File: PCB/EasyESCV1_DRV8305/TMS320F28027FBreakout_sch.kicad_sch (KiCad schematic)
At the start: 1 part, among them U2 TMS320F28027FPTT

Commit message: Finished REV1 Schematic Awaiting Review
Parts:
- added C18: 0.1U, symbol Device:C
- added C19, C20, C21: 2.2n, symbol Device:C
- added C26, C27, C29, C30: 2.2u, symbol Device:C
- added COM: TestPoint, symbol Connector:TestPoint
- added D2: GREEN, symbol Device:LED
- added FB1, FB2: 600, symbol Device:FerriteBead
- added J2: TC2050-IDC, Connector:Tag-Connect_TC2050-IDC-NL_2x05_P1.27mm_Vertical, symbol Connectors:TC2050-IDC
- added R12, R13, R14, R20: 47K, symbol Device:R_US
- added R21: 2.2K, symbol Device:R_US
- added R22: 10K, symbol Device:R_US
- added R23: 330, symbol Device:R_US
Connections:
- net VSEN_PVDD: now reaches U2.10 (ADCINA0_VREFHI)
- net VDDA: now reaches U2.11 (VDDA)
- net VDDA: now also C27.1, FB2.2
- net GND: now reaches U2.12 (VSSA_VREFLO)
- net GND: now also U2.33 (VSS), U2.34 (VREGENZ_N), U2.44 (VSS), U2.45 (X1), C18.2, C19.2, C20.2, C21.2, C26.2, C27.2, C29.2, C30.2, J2.3 (Pin_3), J2.5 (Pin_5), R21.2, R23.2
- net MCU_ISEN_A: now reaches U2.13 (ADCINB1)
- net MCU_ISEN_A: now also C19.1, R12.2
- net MCU_ISEN_B: now reaches U2.15 (ADCINB3)
- net MCU_ISEN_B: now also C20.1, R13.2
- net MCU_ISEN_C: now reaches U2.18 (ADCINB7)
- net MCU_ISEN_C: now also C21.1, R14.2
- net LED: now reaches U2.19 (GPIO34_COMP2OUT)
- net LED: now also D2.2 (A)
- net nTRST: now reaches U2.2 (TRST_N)
- net nTRST: now also J2.9 (Pin_9), R21.1
- net TDI: now reaches U2.20 (GPIO35_TDI)
- net TDI: now also J2.8 (Pin_8)
- net TMS: now reaches U2.21 (GPIO36_TMS)
- net TMS: now also J2.2 (Pin_2)
- net TDO: now reaches U2.22 (GPIO37_TDO)
- net TDO: now also J2.6 (Pin_6)
- net TCK: now reaches U2.23 (GPIO38_XCLKIN_TCK)
- net TCK: now also J2.4 (Pin_4)
- net SCLK: now reaches U2.24 (GPIO18_SPICLKA_SCITXDA_XCLKOUT)
- net COM: now reaches U2.25 (GPIO19_XCLKIN_SPISTEA_SCIRXDA_ECAP1_N)
- net COM: now also COM.1
- net SDO: now reaches U2.26 (GPIO17_SPISOMIA_TZ3_N)
- net SDI: now reaches U2.27 (GPIO16_SPISIMOA_TZ2_N)
- net INL_A: now reaches U2.28 (GPIO1_EPWM1B_COMP1OUT)
- net INH_A: now reaches U2.29 (GPIO0_EPWM1A)
- net nXRS: now reaches U2.3 (XRS_N)
- net nXRS: now also C18.1, R20.2
- net at U2.32 (VDD): now also C29.1
- net VDDIO: now reaches U2.35 (VDDIO)
- net VDDIO: now also C26.1, FB1.2
- net nSCS: now reaches U2.36 (GPIO33_SCLA_EPWMSYNCO_ADCSOCBO_N)
- net INH_B: now reaches U2.37 (GPIO2_EPWM2A)
- net INL_B: now reaches U2.38 (GPIO3_EPWM2B_COMP2OUT)
- net INH_C: now reaches U2.39 (GPIO4_EPWM3A)
- net INL_C: now reaches U2.40 (GPIO5_EPWM3B_ECAP1)
- net EN_GATE: now reaches U2.41 (GPIO6_EPWM4A_EPWMSYNCI_EPWMSYNCO)
- net WAKE: now reaches U2.42 (GPIO7_EPWM4B_SCIRXDA)
- net at U2.43 (VDD): now also C30.1
- net nFAULT: now reaches U2.48 (GPIO28_SCIRXDA_SDAA_TZ2_N)
- net nFAULT: now also R22.2
- net VSEN_A: now reaches U2.6 (ADCINA7)
- net VSEN_B: now reaches U2.7 (ADCINA3)
- net VSEN_C: now reaches U2.8 (ADCINA1)
- new net: D2.1 (K), R23.1
- new net 3.3V: FB1.1, FB2.1, J2.1 (Pin_1), R20.1, R22.1
- new net ISEN_A: R12.1
- new net ISEN_B: R13.1
- new net ISEN_C: R14.1
- no-connect marks 0 -> 13
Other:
- note added: "Current Sense"
- note added: "JTAG"
- note added: "MCU Power"
- note added: "Microcontroller"
- note added: "Reset"
- note added: "Status"
- company: (none) -> Buckley Boards 
- title: (none) -> Easy ESC
- moved on the sheet: U2

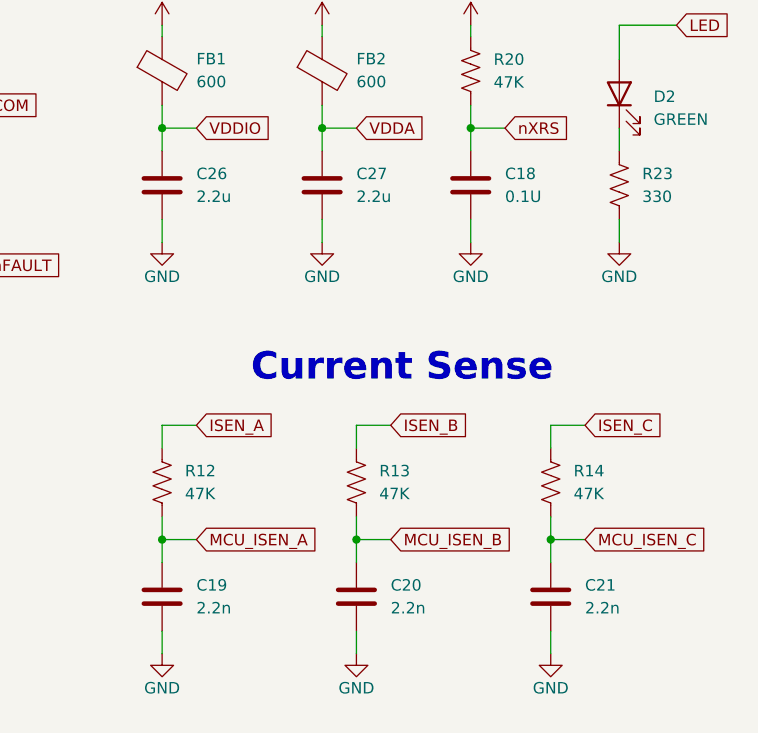
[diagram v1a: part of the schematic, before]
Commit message: Updated Some Errors in Schematic
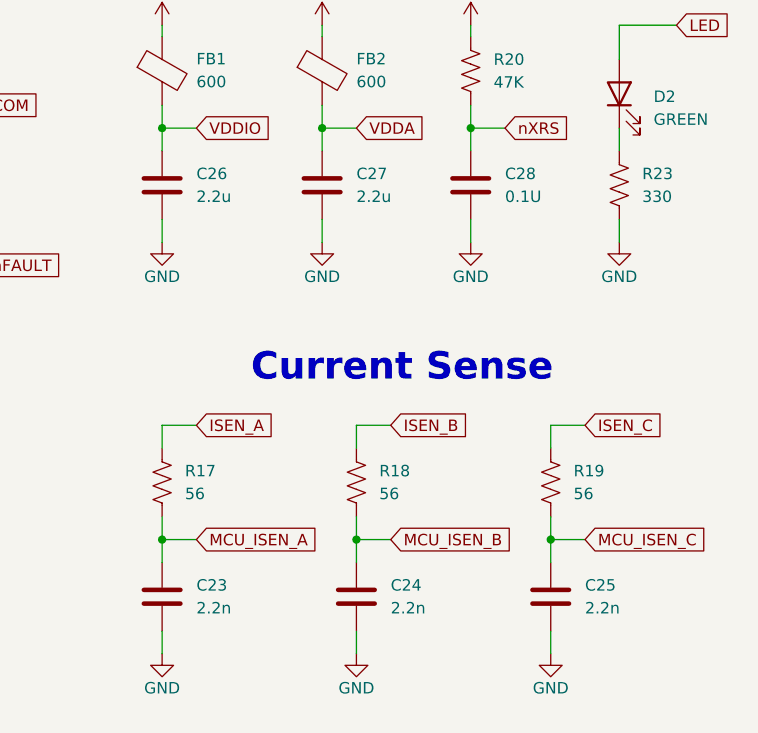
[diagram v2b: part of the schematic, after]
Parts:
- R17: renamed from R12; value 47K -> 56
- R18: renamed from R13; value 47K -> 56
- R19: renamed from R14; value 47K -> 56
- renumbered C19 to C23, C20 to C24, C21 to C25, C18 to C28
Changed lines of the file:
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@@
 		(dnp no)
 		(fields_autoplaced yes)
-		(property "Reference" "R14"
+		(property "Reference" "R19"
 			(at 256.54 128.2699 0)
 			(effects
@@
 			)
 		)
-		(property "Value" "47K"
+		(property "Value" "56"
 			(at 256.54 130.8099 0)
 			(effects
@@
 			(project "EasyESCV1_DRV8305"
 				(path "/6c304649-7c80-4a4c-b925-07b9210ad53d/8049925a-2faa-4187-b86e-b6208aed2e10"
-					(reference "R14")
+					(reference "R19")
 					(unit 1)
 				)
@@
 		(dnp no)
 		(fields_autoplaced yes)
-		(property "Reference" "C19"
+		(property "Reference" "C23"
 			(at 214.63 140.9699 0)
 			(effects
@@
 			(project "EasyESCV1_DRV8305"
 				(path "/6c304649-7c80-4a4c-b925-07b9210ad53d/8049925a-2faa-4187-b86e-b6208aed2e10"
-					(reference "C19")
+					(reference "C23")
 					(unit 1)
 				)
@@
 		(dnp no)
 		(fields_autoplaced yes)
-		(property "Reference" "R13"
+		(property "Reference" "R18"
 			(at 234.95 128.2699 0)
 			(effects
@@
 			)
 		)
-		(property "Value" "47K"
+		(property "Value" "56"
 			(at 234.95 130.8099 0)
 			(effects
@@
 			(project "EasyESCV1_DRV8305"
 				(path "/6c304649-7c80-4a4c-b925-07b9210ad53d/8049925a-2faa-4187-b86e-b6208aed2e10"
-					(reference "R13")
+					(reference "R18")
 					(unit 1)
 				)
@@
 		(dnp no)
 		(fields_autoplaced yes)
-		(property "Reference" "C20"
+		(property "Reference" "C24"
 			(at 236.22 140.9699 0)
 			(effects
@@
 			(project "EasyESCV1_DRV8305"
 				(path "/6c304649-7c80-4a4c-b925-07b9210ad53d/8049925a-2faa-4187-b86e-b6208aed2e10"
-					(reference "C20")
+					(reference "C24")
 					(unit 1)
 				)
@@
 		(dnp no)
 		(fields_autoplaced yes)
-		(property "Reference" "C18"
+		(property "Reference" "C28"
 			(at 248.92 95.2499 0)
 			(effects
@@
 			(project "EasyESCV1_DRV8305"
 				(path "/6c304649-7c80-4a4c-b925-07b9210ad53d/8049925a-2faa-4187-b86e-b6208aed2e10"
-					(reference "C18")
+					(reference "C28")
 					(unit 1)
 				)
@@
 		(dnp no)
 		(fields_autoplaced yes)
-		(property "Reference" "R12"
+		(property "Reference" "R17"
 			(at 213.36 128.2699 0)
 			(effects
@@
 			)
 		)
-		(property "Value" "47K"
+		(property "Value" "56"
 			(at 213.36 130.8099 0)
 			(effects
@@
 			(project "EasyESCV1_DRV8305"
 				(path "/6c304649-7c80-4a4c-b925-07b9210ad53d/8049925a-2faa-4187-b86e-b6208aed2e10"
-					(reference "R12")
+					(reference "R17")
 					(unit 1)
 				)
@@
 		(dnp no)
 		(fields_autoplaced yes)
-		(property "Reference" "C21"
+		(property "Reference" "C25"
 			(at 257.81 140.9699 0)
 			(effects
@@
 			(project "EasyESCV1_DRV8305"
 				(path "/6c304649-7c80-4a4c-b925-07b9210ad53d/8049925a-2faa-4187-b86e-b6208aed2e10"
-					(reference "C21")
-					(unit 1)
-				)
+					(reference "C25")
+					(unit 1)
+				)

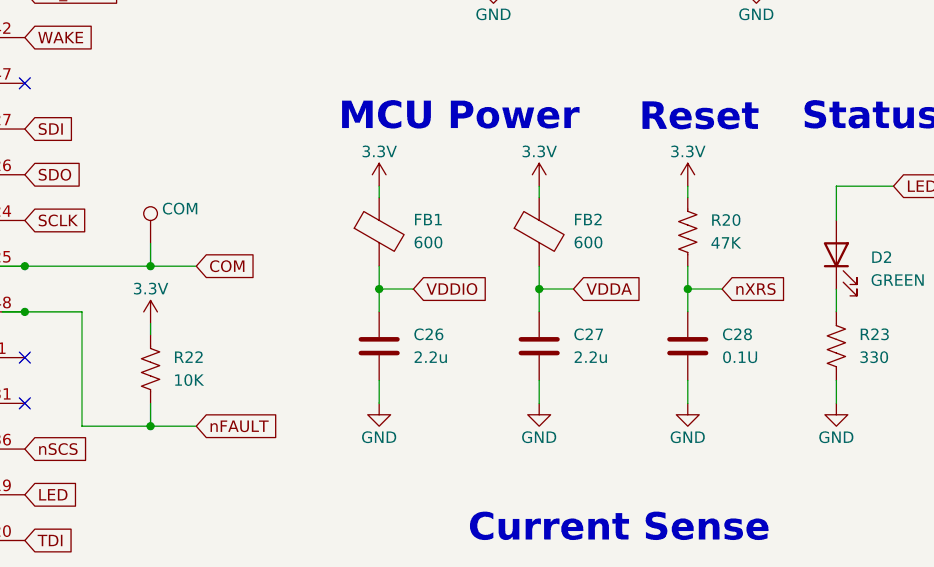
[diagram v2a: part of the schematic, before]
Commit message: Fixed issue with fet symbol and started layout
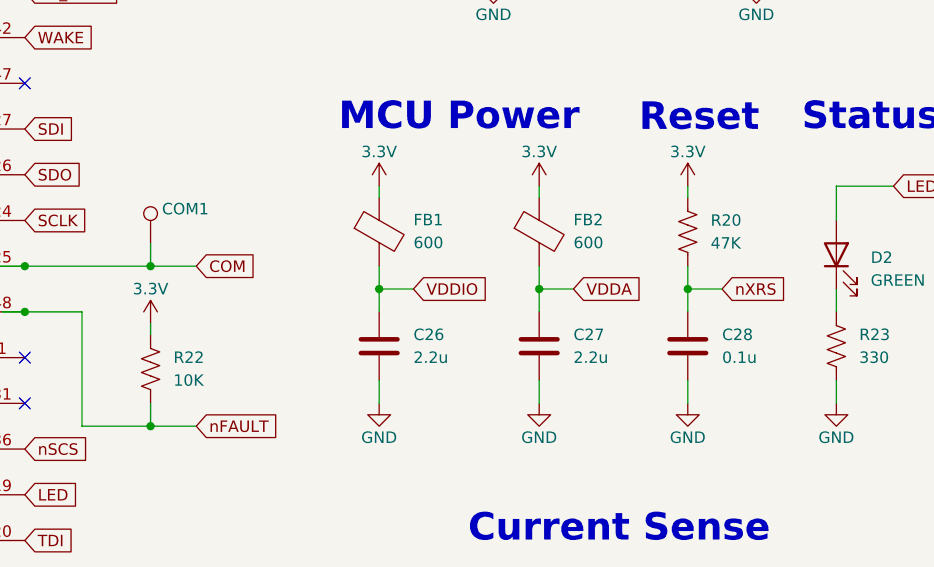
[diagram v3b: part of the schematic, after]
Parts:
- C23, C24, C25: footprint (none) -> Capacitor_SMD:C_0402_1005Metric
- C26, C27, C29, C30: footprint (none) -> Capacitor_SMD:C_0603_1608Metric
- C28: value 0.1U -> 0.1u; footprint (none) -> Capacitor_SMD:C_0402_1005Metric
- COM1: renamed from COM; footprint (none) -> TestPoint:TestPoint_Pad_D3.0mm
- FB1, FB2: footprint (none) -> Inductor_SMD:L_0603_1608Metric
- R17, R18, R19: footprint (none) -> Resistor_SMD:R_0402_1005Metric
- R20, R21, R22, R23: footprint (none) -> Resistor_SMD:R_0603_1608Metric
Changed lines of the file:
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@@
 			)
 		)
-		(property "Footprint" ""
+		(property "Footprint" "Inductor_SMD:L_0603_1608Metric"
 			(at 226.822 83.82 90)
 			(effects
@@
 			)
 		)
-		(property "Footprint" ""
+		(property "Footprint" "Inductor_SMD:L_0603_1608Metric"
 			(at 209.042 83.82 90)
 			(effects
@@
 			)
 		)
-		(property "Footprint" ""
+		(property "Footprint" "Resistor_SMD:R_0402_1005Metric"
 			(at 255.016 129.794 90)
 			(effects
@@
 			)
 		)
-		(property "Footprint" ""
+		(property "Footprint" "Capacitor_SMD:C_0603_1608Metric"
 			(at 211.7852 100.33 0)
 			(effects
@@
 			)
 		)
-		(property "Footprint" ""
+		(property "Footprint" "Resistor_SMD:R_0603_1608Metric"
 			(at 186.436 99.314 90)
 			(effects
@@
 			)
 		)
-		(property "Footprint" ""
+		(property "Footprint" "Resistor_SMD:R_0603_1608Metric"
 			(at 262.636 96.774 90)
 			(effects
@@
 		(on_board yes)
 		(dnp no)
-		(property "Reference" "COM"
+		(property "Reference" "COM1"
 			(at 186.69 81.28 0)
 			(effects
@@
 			)
 		)
-		(property "Footprint" ""
+		(property "Footprint" "TestPoint:TestPoint_Pad_D3.0mm"
 			(at 190.5 85.09 0)
 			(effects
@@
 			(project "EasyESCV1_DRV8305"
 				(path "/6c304649-7c80-4a4c-b925-07b9210ad53d/8049925a-2faa-4187-b86e-b6208aed2e10"
-					(reference "COM")
+					(reference "COM1")
 					(unit 1)
 				)
@@
 			)
 		)
-		(property "Footprint" ""
+		(property "Footprint" "Capacitor_SMD:C_0402_1005Metric"
 			(at 211.7852 146.05 0)
 			(effects
@@
 			)
 		)
-		(property "Footprint" ""
+		(property "Footprint" "Resistor_SMD:R_0402_1005Metric"
 			(at 233.426 129.794 90)
 			(effects
@@
 			)
 		)
-		(property "Footprint" ""
+		(property "Footprint" "Capacitor_SMD:C_0402_1005Metric"
 			(at 233.3752 146.05 0)
 			(effects
@@
 			)
 		)
-		(property "Footprint" ""
+		(property "Footprint" "Capacitor_SMD:C_0603_1608Metric"
 			(at 229.5652 100.33 0)
 			(effects
@@
 			)
 		)
-		(property "Footprint" ""
+		(property "Footprint" "Capacitor_SMD:C_0603_1608Metric"
 			(at 31.4452 39.37 0)
 			(effects
@@
 			)
 		)
-		(property "Value" "0.1U"
+		(property "Value" "0.1u"
 			(at 248.92 97.7899 0)
 			(effects
@@
 			)
 		)
-		(property "Footprint" ""
+		(property "Footprint" "Capacitor_SMD:C_0402_1005Metric"
 			(at 246.0752 100.33 0)
 			(effects
@@
 			)
 		)
-		(property "Footprint" ""
+		(property "Footprint" "Capacitor_SMD:C_0603_1608Metric"
 			(at 20.0152 36.83 0)
 			(effects
@@
 			)
 		)
-		(property "Footprint" ""
+		(property "Footprint" "Resistor_SMD:R_0402_1005Metric"
 			(at 211.836 129.794 90)
 			(effects
@@
 			)
 		)
-		(property "Footprint" ""
+		(property "Footprint" "Capacitor_SMD:C_0402_1005Metric"
 			(at 254.9652 146.05 0)
 			(effects
@@
 			)
 		)
-		(property "Footprint" ""
+		(property "Footprint" "Resistor_SMD:R_0603_1608Metric"
 			(at 246.126 84.074 90)
 			(effects
@@
 			)
 		)
-		(property "Footprint" ""
+		(property "Footprint" "Resistor_SMD:R_0603_1608Metric"
 			(at 253.746 51.054 90)
 			(effects
